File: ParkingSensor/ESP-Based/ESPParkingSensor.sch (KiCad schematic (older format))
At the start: 10 parts, among them P1 CONN_UART, P2 CONN_WS2812, P3 CONN_01X02, P4 CONN_US, U1 ESP-12E, U2 AP1117

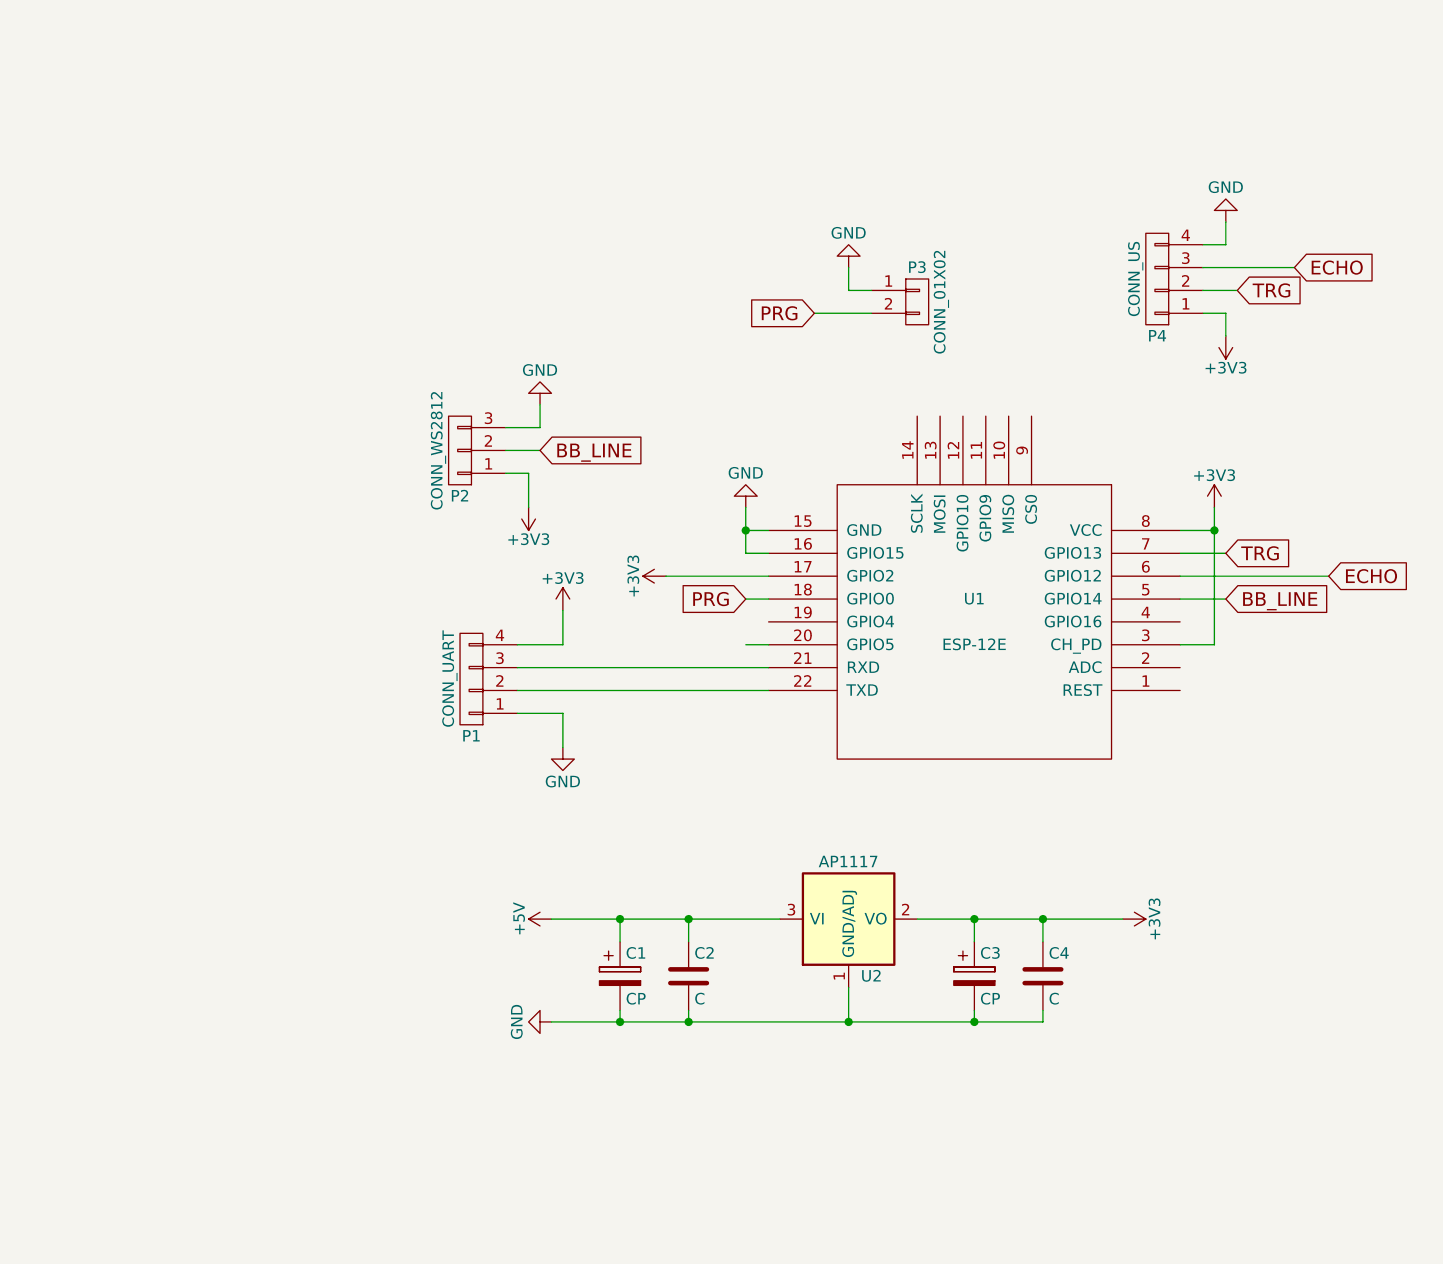
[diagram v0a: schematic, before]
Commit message: changed the braces to be in the right place on loop() and setup()
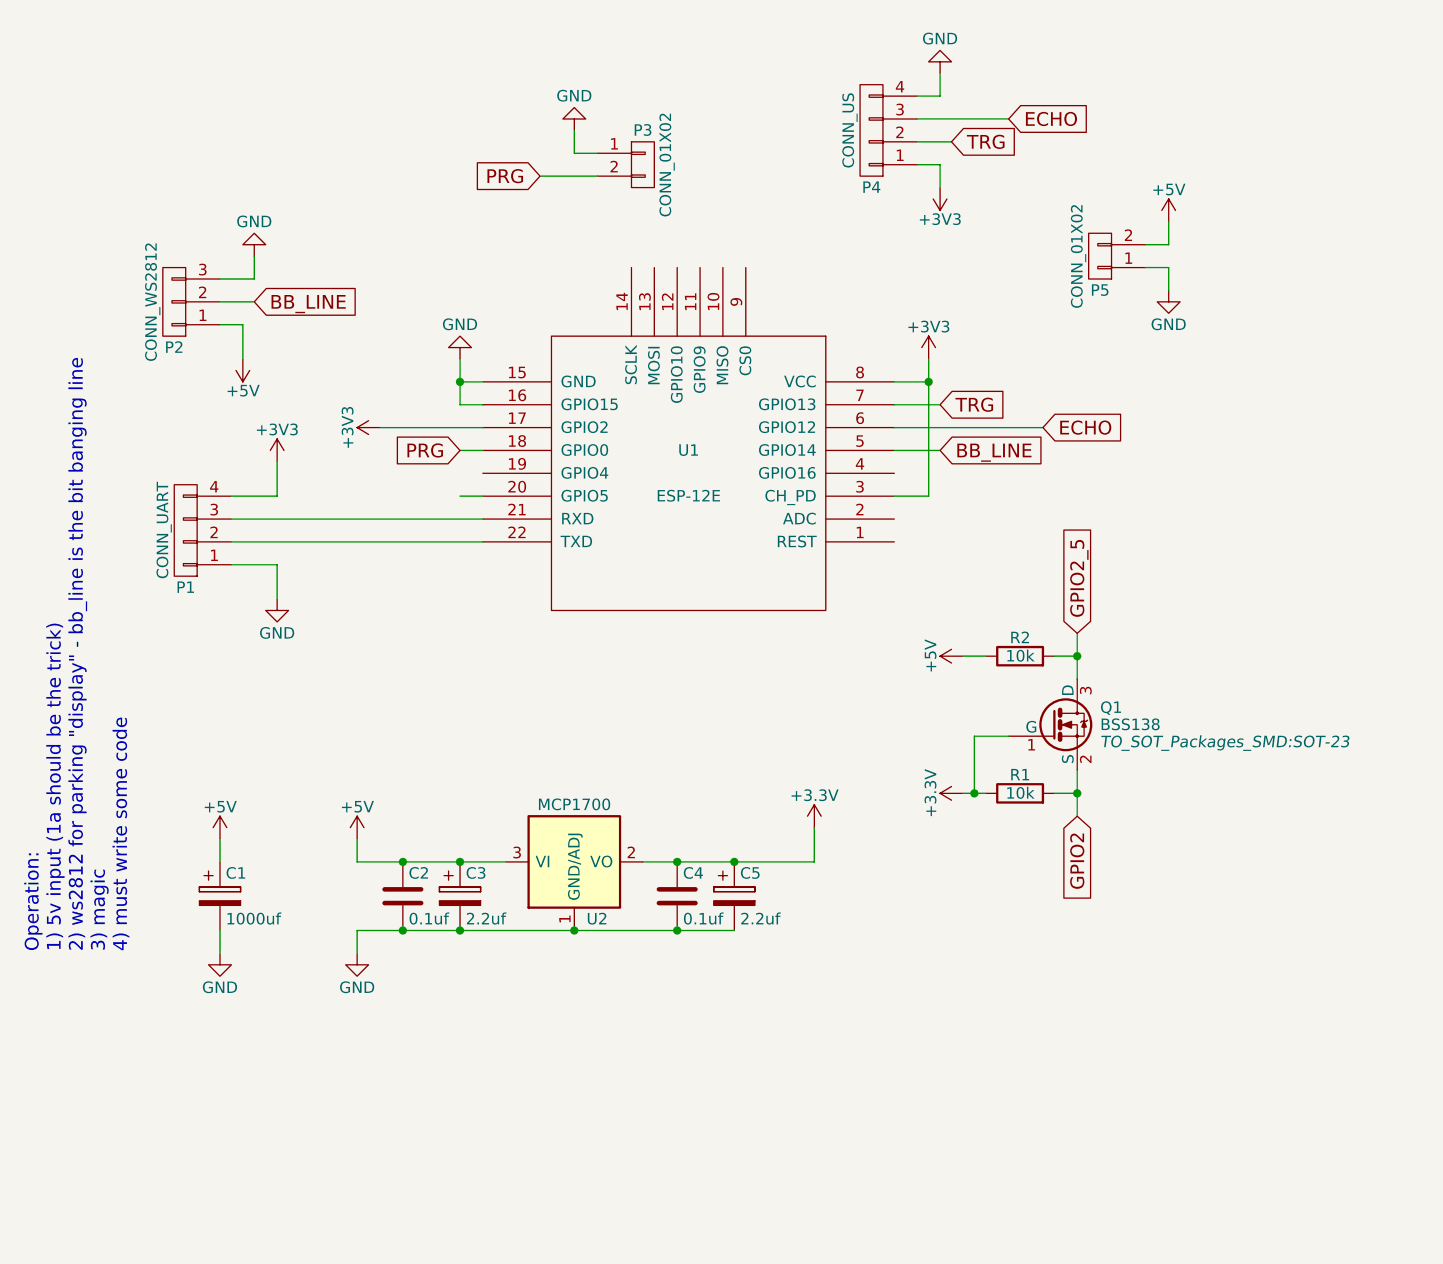
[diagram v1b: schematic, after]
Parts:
- added C5: 2.2uf, SMD_Packages:SMD-1210_Pol, symbol CP
- added P5: CONN_01X02, Pin_Headers:Pin_Header_Straight_1x02, symbol CONN_01X02
- added Q1: BSS138, TO_SOT_Packages_SMD:SOT-23, symbol BSS138
- added R1, R2: 10k, Resistors_SMD:R_0805_HandSoldering, symbol R
- C1: value CP -> 1000uf; footprint SMD_Packages:SMD-1210_Pol -> Capacitors_ThroughHole:C_Radial_D6.3_L11.2_P2.5; Notes (none) -> Basically a big cap for powering lights
- C2: value C -> 0.1uf; Comments (none) -> a cap of around 0.1 to 10 uf - anything in that range will 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
- C3: value CP -> 2.2uf; Notes (none) -> a Tant cap in the 1-10uf range - anything that fits will do
- C4: value C -> 0.1uf; Notes (none) -> Any cap in the 0.1-10uf range
- U2: value AP1117 -> MCP1700; footprint so23-8:SOT-223 -> TO_SOT_Packages_SMD:SOT-23
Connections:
- net +3V3: now also C5.1, Q1.1 (G), R1.1; no longer C3.1, P2.1 (P1)
- net +5V: now also C3.1, P2.1 (P1), P5.2 (P2), R2.1
- net GND: now also C5.2, P5.1 (P1)
- new net GPIO2: Q1.2 (S), R1.2
- new net GPIO2_5: Q1.3 (D), R2.2
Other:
- note added: "Operation:\n1) 5v input (1a should be the trick)\n2) ws2812 for parking "display" - bb_line is the bit banging line\n3) magic\n4) must write some code"
- moved on the sheet: P1, P2, P3, P4, U1

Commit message: forgot to route thru the level converter
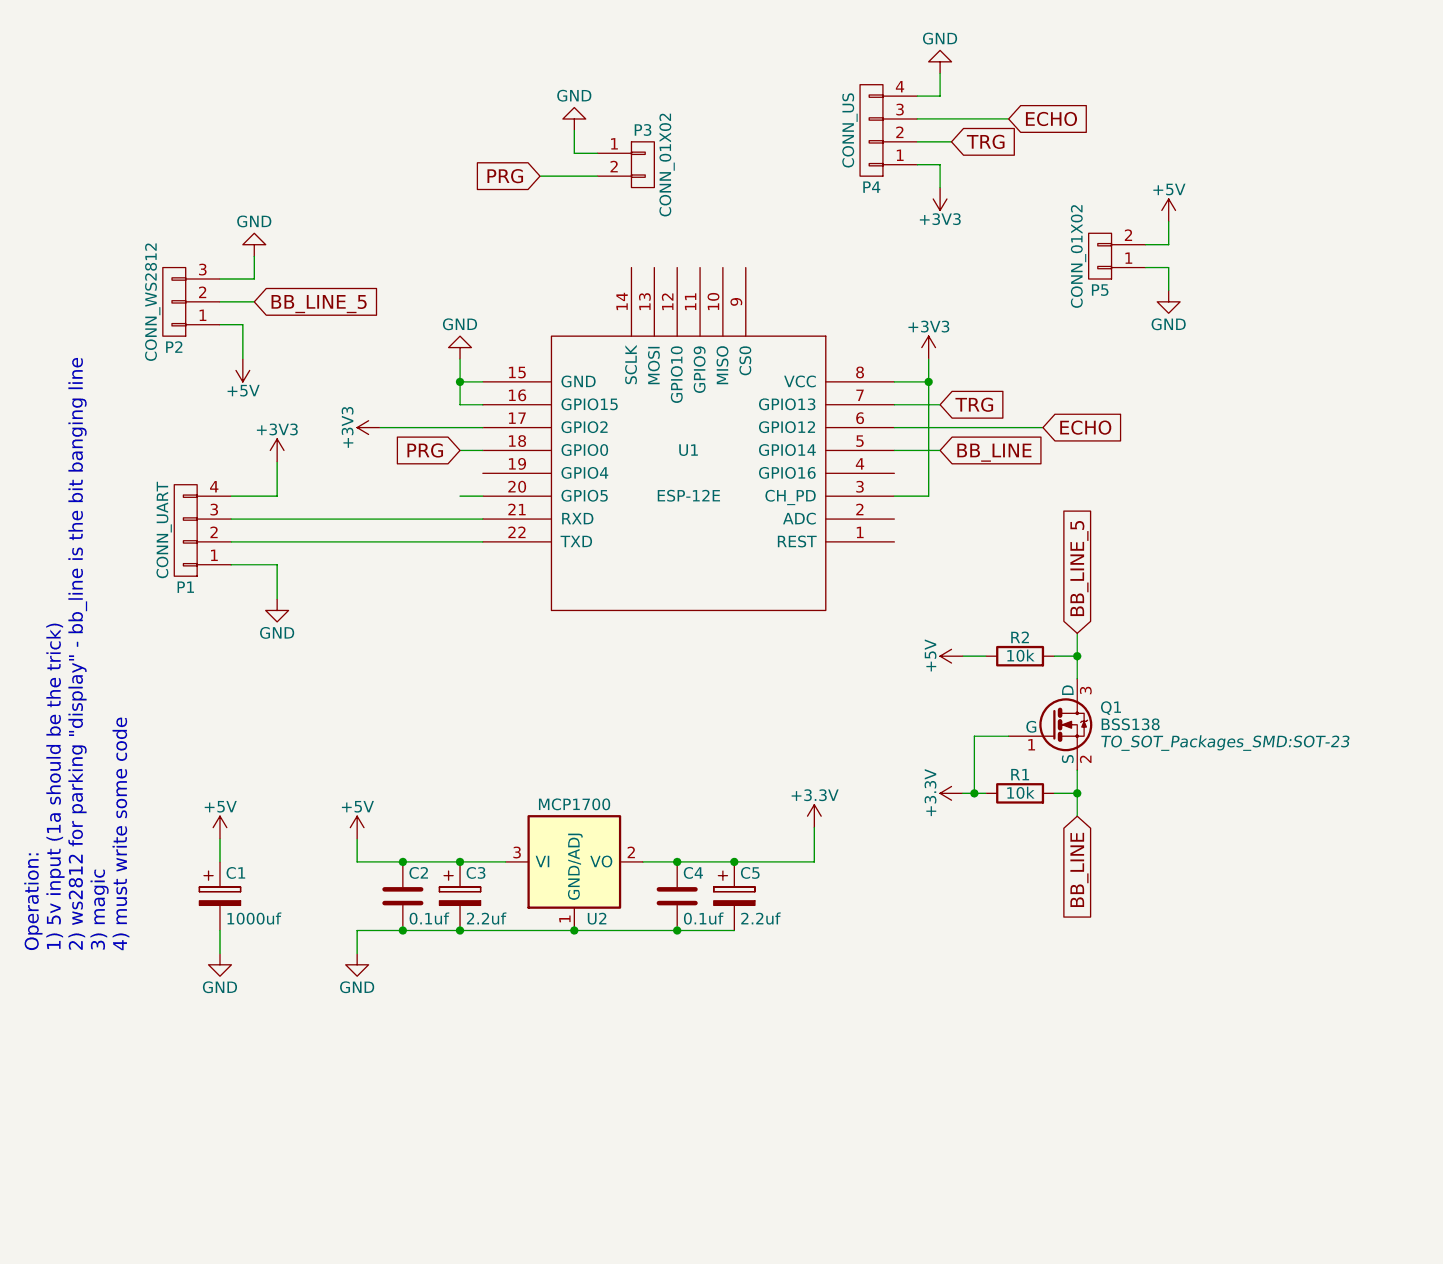
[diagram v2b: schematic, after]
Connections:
- net GPIO2 is gone; now on net BB_LINE: Q1.2 (S), R1.2
- net BB_LINE: no longer P2.2 (P2)
- net GPIO2_5 renamed BB_LINE_5
- net BB_LINE_5: now also P2.2 (P2)
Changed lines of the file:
@@
 LIBS:ESP8266
 LIBS:ESPParkingSensor-cache
-LIBS:esp-ws2812-cache
 EELAYER 25 0
 EELAYER END
@@
 Connection ~ 4150 2000
 Text GLabel 1200 1650 2    60   Input ~ 0
-BB_LINE
+BB_LINE_5
 Text GLabel 4200 2300 2    60   Input ~ 0
 BB_LINE
@@
 	1    0    0    -1
 $EndComp
-Text GLabel 4800 3900 3    60   Input ~ 0
-GPIO2
 Text GLabel 4800 3100 1    60   Input ~ 0
-GPIO2_5
+BB_LINE_5
 $Comp
 L +3.3V #PWR014
@@
 	-1   0    0    1
 $EndComp
+Text GLabel 4800 3900 3    60   Input ~ 0
+BB_LINE
 $EndSCHEMATC

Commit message: moved to 5v hc-sr04 simplified
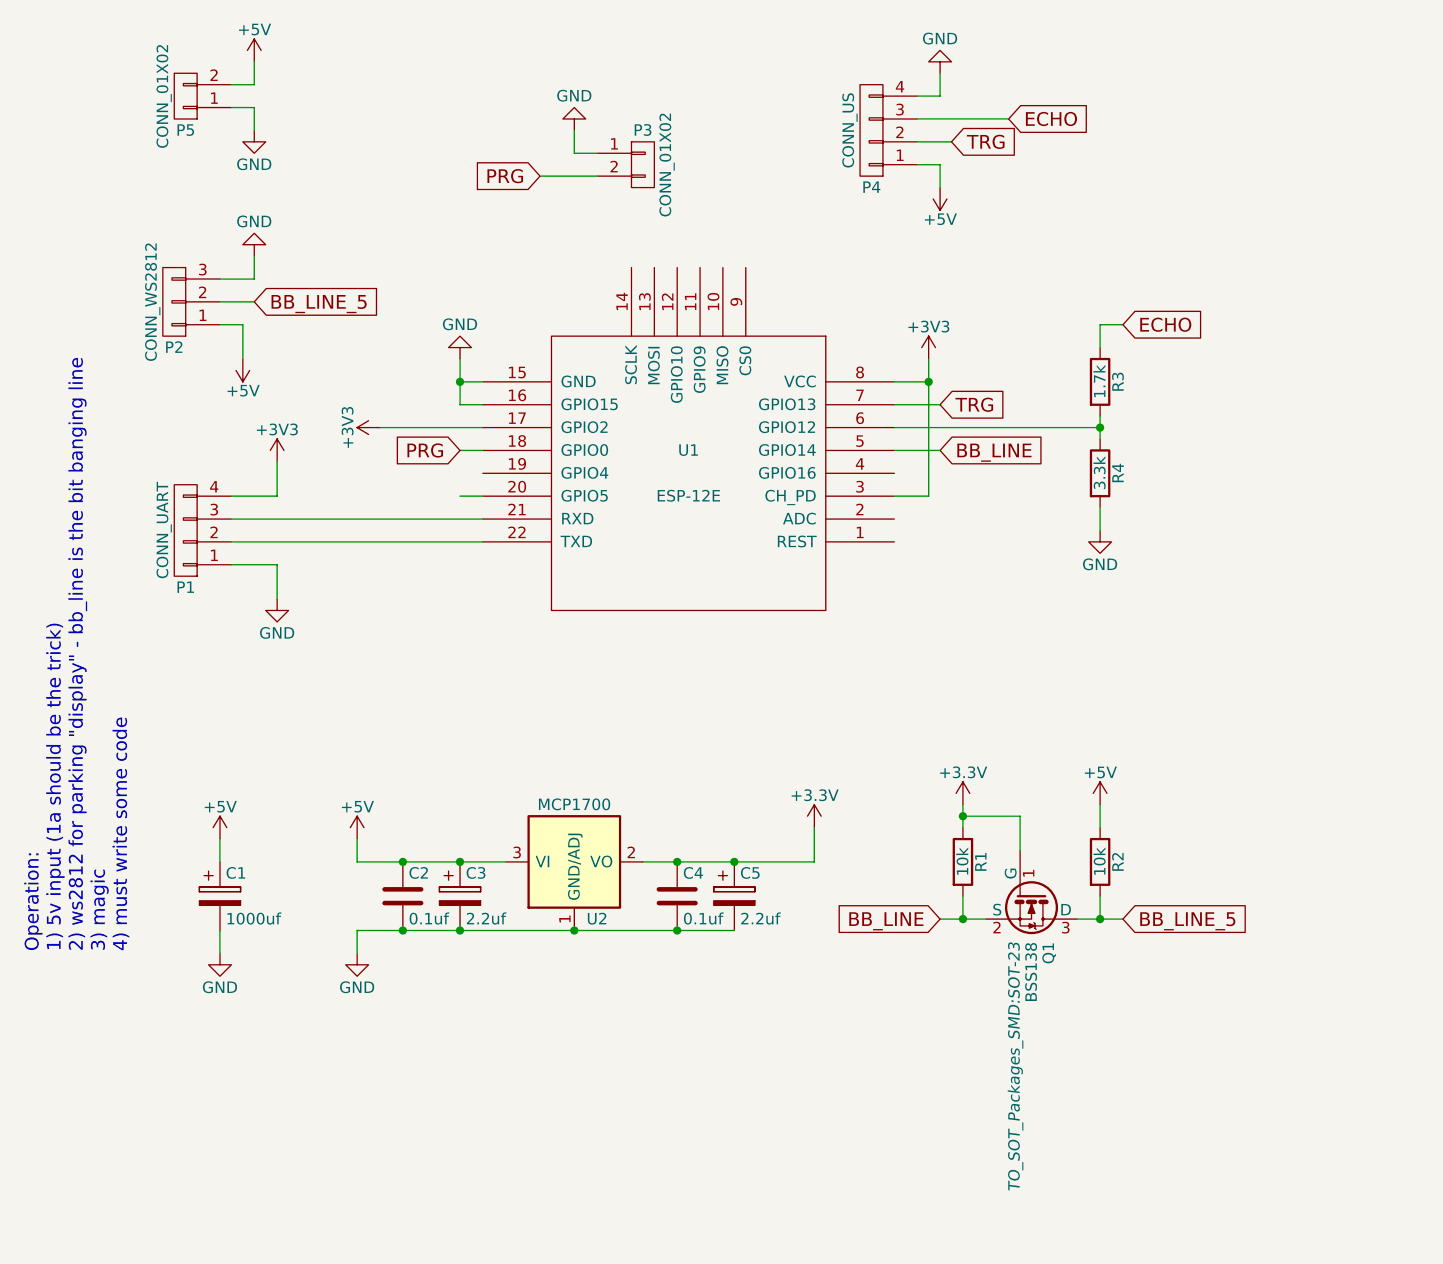
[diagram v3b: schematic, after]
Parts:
- added R3: 1.7k, Resistors_SMD:R_0805_HandSoldering, symbol R
- added R4: 3.3k, Resistors_SMD:R_0805_HandSoldering, symbol R
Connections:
- net +3V3: no longer P4.1 (P1)
- net +5V: now also P4.1 (P1)
- net ECHO: now also R3.1; no longer U1.6 (GPIO12)
- net GND: now also R4.2
- new net: R3.2, R4.1, U1.6 (GPIO12)
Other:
- moved on the sheet: P5, Q1, R1, R2
